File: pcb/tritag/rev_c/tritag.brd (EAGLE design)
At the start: 64.4 x 71.8 mm, 138 parts, among them J1 TC2030-JLINK-NL, J3 MICRO_USB_B_HIROSE_ZX62-B-5PA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, J4 BAT_HOLE, J5 BAT_HOLE, J6 TC2030-JLINK-NL, J7 CON_MICRO_SDDM3AT-SF-PEJM5, T1 HHM1595A1, U1 NRF52840, U12 SIP32510, U2 MCP73831, U3 FT232RQ, U4 MAX8887EZK33+T, U5 STM32F091CC, U6 SKY13317, U7 LXDC2HN18A, U8 DW1000, U9 LIS2DW12, X1 32MHz, X2 38.4M, X3 16M, X4 32.768kHz

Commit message: carrier board ready for layout
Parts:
- removed D3: SML-LX0404SIUPGUSB, leds:1MM_SQ_4PAD
- removed J6: TC2030-JLINK-NL, connector:TC2030-IDC-NL
- removed R15: 1k, passives:0402_RES
- removed R16: 100k, passives:0201_RES
- removed SJ2, SJ3, SJ4, SJ5: SOLDERJUMPERNC2, SparkFun-Passives:SJ_2S-NOTRACE
- added D2: SML-LX0404SIUPGUSB, leds:1MM_SQ_4PAD
- added GPIO0, GPIO1: TEST_POINT_0.040IN, headers:TESTPOINT_0.040IN
- added J2: TC2030-JLINK-NL, connector:TC2030-IDC-NL
- added R1: 270, passives:0402_RES
- added R6: 16k, passives:0402_RES
- added TP13, TP14: TEST-POINT, headers:PAD.03X.03
- added U$2: (no value), logos:UCB_CAL_50MIL
- C18, C21, C58: device passives:0603_CAP -> passives:0402_CAP
- C20, C22, C23, C24, C25, C26, C27, C28, C29, C30, C31, C32, C33, C34, C35, C36, C37, C38, C39, C40, C41, C42, C43, C44, C45, C46, C47, C48, C49, C50, C51, C52, C57: device passives:0201_CAP -> passives:0402_CAP
- C53: value 100nF -> 4.7uF; device passives:0201_CAP -> passives:0402_CAP
- C54: value 4.7uF -> 100nF; device passives:0201_CAP -> passives:0402_CAP
- C55: value 10nF -> 1uF; device passives:0201_CAP -> passives:0402_CAP
- C56: value 1uF -> 10nF; device passives:0201_CAP -> passives:0402_CAP
- R10: value 16k -> 11k; device passives:0201_RES -> passives:0402_RES
- R11, R12: value 11k -> 1k; device passives:0201_RES -> passives:0402_RES
- R14: value 1k -> 100k
- R9: value 270 -> 11k 1%; device passives:0201_RES -> passives:0402_RES
- TP5, TP6: value TEST_POINT_0.040IN -> TEST-POINT; device headers:TESTPOINT_0.040IN -> headers:PAD.03X.03
- moved A5 280.6 mm to (78.5, 29.1)
- moved A2.1 273.8 mm to (92.1, 29.1)
- moved A2 273.5 mm to (85.2, 29.1)
- moved C60 246.6 mm to (79.2, -15.7)
- moved A4 221.7 mm to (72.1, -7.49)
- moved C1 221.7 mm to (85.5, -10.3)
- moved C12 221.7 mm to (78.2, -6.73)
- moved C14 221.7 mm to (81.8, -6.73)
- moved C2 221.7 mm to (71.4, -13.1)
- moved C3 221.7 mm to (74.0, -13.1)
- moved C4 221.7 mm to (76.7, -13.1)
- moved C5 221.7 mm to (79.4, -13.1)
- moved C6 221.7 mm to (82.0, -13.1)
- moved C7 221.7 mm to (84.7, -13.1)
- moved C78 221.7 mm to (85.3, -6.73)
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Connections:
- removed net !FTDI_RESET: SJ3.2, U3.18
- removed net FTDI_VCCIO: SJ2.2, U3.1
- removed net N$28: D3.3, R15.1
- removed net N$29: D3.2, R13.1
- removed net RXD: SJ4.1, U3.2
- removed net TXD: SJ5.1, U3.30
- removed net VBAT_OK: U1.R24
- removed net VCC: C1.1, C11.1, C2.1, C3.1, C5.1, C6.1, C75.1, C76.1, D5.1, J1.1, R4.2, R5.2, SJ2.1, U1.A22, U1.AD14, U1.AD23, U1.B1, U1.W1, U1.Y2, U12.5, U12.6, U4.5, U9.10, U9.9
- new net N$12: C42.1, R6.2
- new net N$14: C44.1, R1.1, U8.12
- new net N$16: C43.1, R6.1, U8.8
- new net N$8: C41.1, R1.2
- new net NRF_GPIO_0: TP13.P$1, U1.AC11
- new net NRF_GPIO_1: TP14.P$1, U1.AD12
- new net NRF_SWO: J1.6, U1.AD22
- net !RST: now also U3.18; no longer SJ3.1
- net !STM_RST: now also J2.3; no longer J6.3
- net +1V8: now also C20.1, C24.1; no longer C20.P$1, C24.P$1
- net +3V3: now also C1.1, C11.1, C2.1, C3.1, C31.1, C32.1, C33.1, C34.1, C35.1, C36.1, C37.1, C38.1, C39.1, C40.1, C49.1, C5.1, C50.1, C51.1, C52.1, C53.1, C54.1, C55.1, C56.1, C6.1, C75.1, C76.1, D2.1, D5.1, J1.1, J2.1, R4.2, R5.2, U1.A22, U1.AD14, U1.AD23, U1.B1, U1.W1, U1.Y2, U12.5, U12.6, U3.1, U4.5, U9.10, U9.9; no longer C31.P$1, C32.P$1, C33.P$1, C34.P$1, C35.P$1, C36.P$1, C37.P$1, C38.P$1, C39.P$1, C40.P$1, C49.P$1, C50.P$1, C51.P$1, C52.P$1, C53.P$1, C54.P$1, C55.P$1, C56.P$1, D3.1, J6.1
- net DBG_RX: now also U3.30; no longer SJ5.2
- net DBG_TX: now also U3.2; no longer SJ4.2
- net DW_IRQ: now also R14.2; no longer R16.2
- net EXT_I2C_SCL: now also U1.AD8; no longer U1.A20, U1.AC9
- net EXT_I2C_SDA: no longer U1.B19
- net GND: now also C20.2, C22.2, C23.2, C24.2, C25.2, C26.2, C27.2, C28.2, C29.2, C30.2, C31.2, C32.2, C33.2, C34.2, C35.2, C36.2, C37.2, C38.2, C39.2, C40.2, C41.2, C42.2, C43.2, C44.2, C45.2, C46.2, C47.2, C48.2, C49.2, C50.2, C51.2, C52.2, C53.2, C54.2, C55.2, C56.2, C57.2, J2.5, R10.2, R14.1, R9.1, TP10.P$1; no longer C20.P$2, C22.P$2, C23.P$2, C24.P$2, C25.P$2, C26.P$2, C27.P$2, C28.P$2, C29.P$2, C30.P$2, C31.P$2, C32.P$2, C33.P$2, C34.P$2, C35.P$2, C36.P$2, C37.P$2, C38.P$2, C39.P$2, C40.P$2, C41.P$2, C42.P$2, C43.P$2, C44.P$2, C45.P$2, C46.P$2, C47.P$2, C48.P$2, C49.P$2, C50.P$2, C51.P$2, C52.P$2, C53.P$2, C54.P$2, C55.P$2, C56.P$2, C57.P$2, J6.5, R11.1, R12.2, R16.1, TP12.P$1
- net GPIO0: now also GPIO0.TESTPOINT; no longer TP5.TESTPOINT
- net GPIO1: now also GPIO1.TESTPOINT; no longer TP6.TESTPOINT
- net GPIO2: now also TP5.P$1, U5.29; no longer TP7.P$1, U5.21
- net GPIO3: now also TP6.P$1, U5.28; no longer TP8.P$1, U5.22
- net LED_BLUE: now also R13.2; no longer R15.2, TP10.P$1
- net LED_GREEN: now also R12.2, U5.41; no longer R14.2, TP9.P$1, U5.39
- net LED_RED: now also R11.2, U5.39; no longer R13.2, TP11.P$1, U5.41
- net N$21: now also U8.5; no longer C41.P$1
- net N$22: now also R10.1, U5.44; no longer C42.P$1, R10.2
- net N$23: now also D2.4, R12.1, TP7.P$1; no longer C44.P$1, R9.1, U8.12
- net N$24: now also D2.3, R13.1, TP9.P$1; no longer C43.P$1, R10.1, U8.8
- net N$25: now also D2.2, R11.1, TP8.P$1; no longer R11.2, U8.5
- net N$26: now also TP11.P$1, U8.36; no longer R12.1, U5.44
- net N$27: now also TP12.P$1, U8.35; no longer D3.4, R14.1
- net OSC_IN: now also C47.1; no longer C47.P$1
- net OSC_OUT: now also C48.1; no longer C48.P$1
- net STM_INTERRUPT: now also U1.AC21; no longer U1.B17
- net STM_SWCLK: now also J2.4; no longer J6.4
- net STM_SWDIO: now also J2.2; no longer J6.2
- net VDDCLK: now also C26.1; no longer C26.P$1
- net VDDDIG: now also C22.1, C23.1; no longer C22.P$1, C23.P$1
- net VDDIF: now also C29.1; no longer C29.P$1
- net VDDIO: now also C28.1, C57.1; no longer C28.P$1, C57.P$1
- net VDDMS: now also C25.1; no longer C25.P$1
- net VDDSYN: now also C27.1; no longer C27.P$1
- net VDDVCO: now also C30.1; no longer C30.P$1
- net XTAL1: now also C46.1; no longer C46.P$1
- net XTAL2: now also C45.1; no longer C45.P$1
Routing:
- net +3V3: track 87.1 -> 256.6 mm, vias 5 -> 13
- net VCC: track 50.8 -> 0.00 mm, vias 4 -> 0
- net VBAT: track 46.7 -> 0.00 mm
- net N$5: track 28.2 -> 0.00 mm, vias 3 -> 0
- net VUSB: track 24.1 -> 0.00 mm, vias 1 -> 0
- net EXT_I2C_SCL: track 20.4 -> 0.00 mm, vias 1 -> 0
- net EXT_I2C_SDA: track 19.4 -> 0.00 mm, vias 1 -> 0
- net STM_INTERRUPT: track 17.6 -> 0.00 mm, vias 1 -> 0
- net LED_RED: track 14.8 -> 1.69 mm, vias 2 -> 0
- net LED_BLUE: track 13.5 -> 1.48 mm, vias 2 -> 0
- net LED_GREEN: track 12.2 -> 1.37 mm, vias 2 -> 0
- net GND: track 96.6 -> 105.1 mm, vias 46 -> 204
- net RF2: track 7.93 -> 15.4 mm
- net RF1: track 6.40 -> 13.8 mm
- net N$16: track 0.00 -> 4.89 mm
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- added copper zone on layer 1, net N$3
- added copper zone on layer 1, net RF3
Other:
- board size 64.4 x 71.8 mm -> 66 x 48.9 mm
- board text added: "17/07/2018"
- board text added: "Andreas Biri, Pat Pannuto"
- board text added: "C"
- board text added: "G"
- board text added: "GND"
- board text added: "IO2"
- board text added: "IO3"
- board text added: "R"
- board text added: "SquarePoint"
- board text added: "v3.1"
- board text removed: "13/07/2018"
- board text removed: "2018/07/14"
- board text removed: "Andreas Biri"

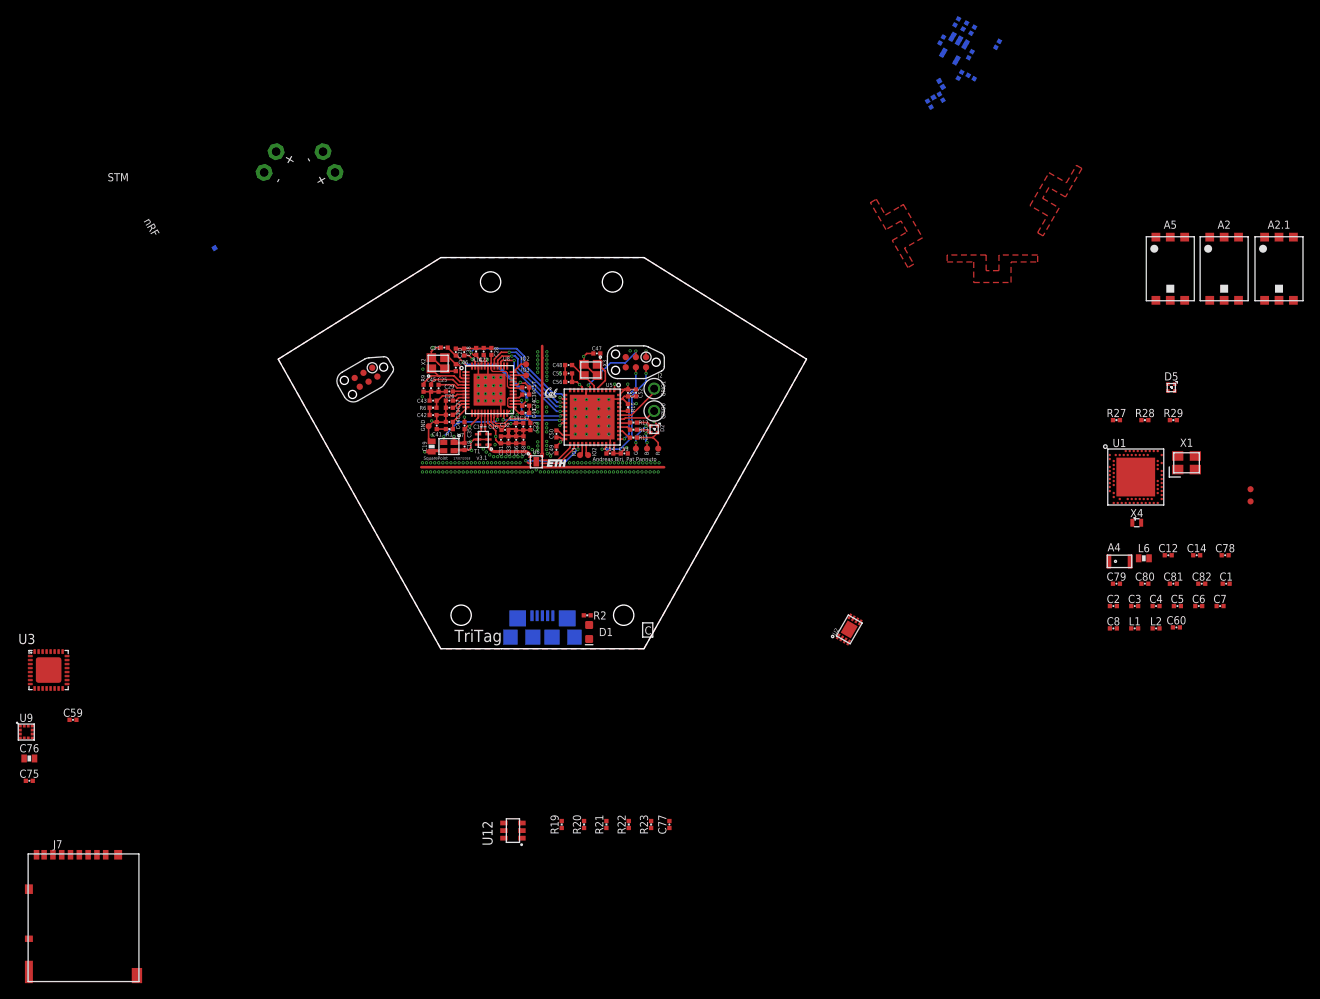
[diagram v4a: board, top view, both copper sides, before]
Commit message: Carrier ready for routing
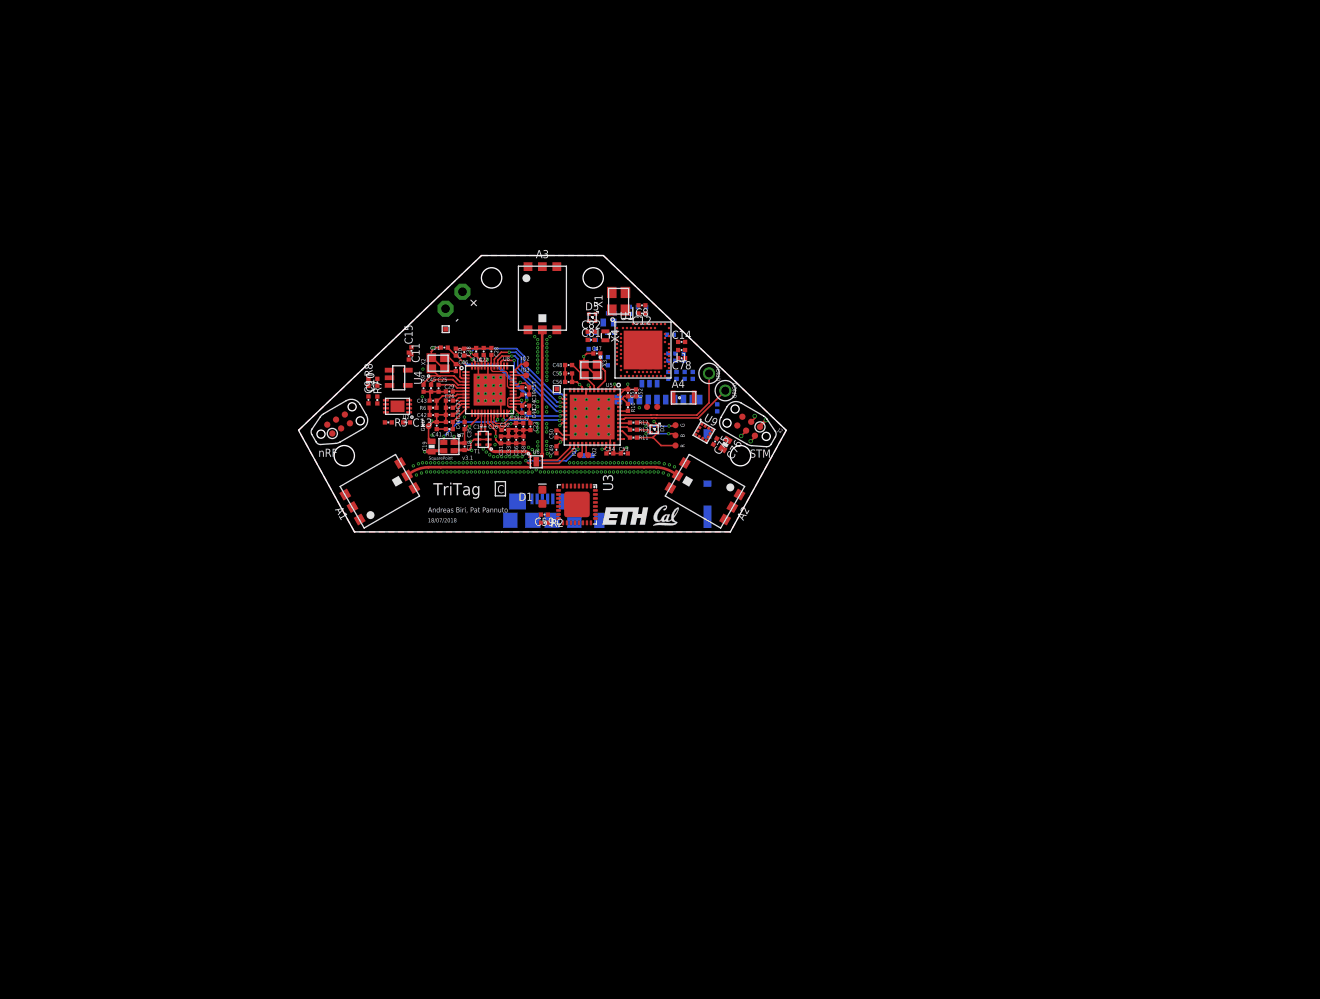
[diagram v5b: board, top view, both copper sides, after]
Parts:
- removed A2.1, A5: TAIYO-YUDEN-AH086M, chips:TAIYO-YUDEN-AH086M
- removed J4: BAT_HOLE, connector:BATTERY_HOLE
- removed R4, R5: DNP, passives:0402_RES
- removed U$1: (no value), logos:ETH_100MIL
- removed U$2: (no value), logos:UCB_CAL_50MIL
- added A1, A3: TAIYO-YUDEN-AH086M, chips:TAIYO-YUDEN-AH086M
- added U$3: (no value), logos:ETH_200MIL
- added U$4: (no value), logos:UCB_CAL_100MIL
- moved C75 95.6 mm to (21.6, 7.49), turned to 240 degrees
- moved C76 95.4 mm to (22.9, 7.11), turned to 240 degrees
- moved U9 92.6 mm to (20.2, 8.64), turned to 330 degrees
- moved J7 91.8 mm to (14.2, 12.8), flipped to the bottom
- moved C10 88.3 mm to (-20.6, 14.9), flipped to the top, turned to 90 degrees
- moved R8 87.4 mm to (-21.7, 14.9), flipped to the top, turned to 270 degrees
- moved C9 87.4 mm to (-21.7, 12.7), flipped to the top, turned to 90 degrees
- moved R7 87.1 mm to (-20.6, 12.7), flipped to the top, turned to 90 degrees
- moved R3 83.6 mm to (-19.3, 9.87), flipped to the top, turned to 180 degrees
- moved C13 82.7 mm to (-17.0, 9.87), flipped to the top, turned to 180 degrees
- moved C82 82.6 mm to (6.10, 21.2)
- moved C1 82.0 mm to (10.9, 23.9), flipped to the bottom, turned to 90 degrees
- moved U4 80.7 mm to (-18.0, 15.5), flipped to the top, turned to 270 degrees
- moved C6 80.5 mm to (7.75, 18.0), flipped to the bottom
- moved C15 79.1 mm to (-16.4, 18.8), flipped to the top, turned to 90 degrees
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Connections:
- removed net INTERRUPT: U5.12
- net +3V3: no longer R4.2, R5.2
- net EXT_I2C_SCL: no longer R5.1
- net EXT_I2C_SDA: no longer R4.1
- net GND: no longer J4.N
- net RF1: now also A1.A; no longer A5.A
- net RF2: now also A2.A; no longer A2.1.A
- net RF3: now also A3.A; no longer A2.A
- net STM_INTERRUPT: now also U5.12
- net VBAT: no longer J4.P
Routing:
- net +3V3: track 256.6 -> 227.1 mm
- net !STM_RST: track 9.28 -> 25.7 mm
- net GPIO0: track 4.79 -> 14.7 mm
- net GPIO1: track 6.02 -> 15.6 mm
- net STM_SWCLK: track 10.2 -> 17.3 mm, vias 2 -> 1
- net STM_SWDIO: track 14.8 -> 21.1 mm
- net GND: track 105.1 -> 102.8 mm, vias 204 -> 219
- net RF1: track 13.8 -> 15.8 mm
- net RF3: track 13.9 -> 15.9 mm
- net RF2: track 15.4 -> 17.3 mm
- net N$24: track 4.43 -> 6.29 mm
- net N$25: track 4.53 -> 6.10 mm
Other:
- board size 66 x 48.9 mm -> 61 x 34.5 mm
- board text added: "18/07/2018"
- board text removed: "17/07/2018"

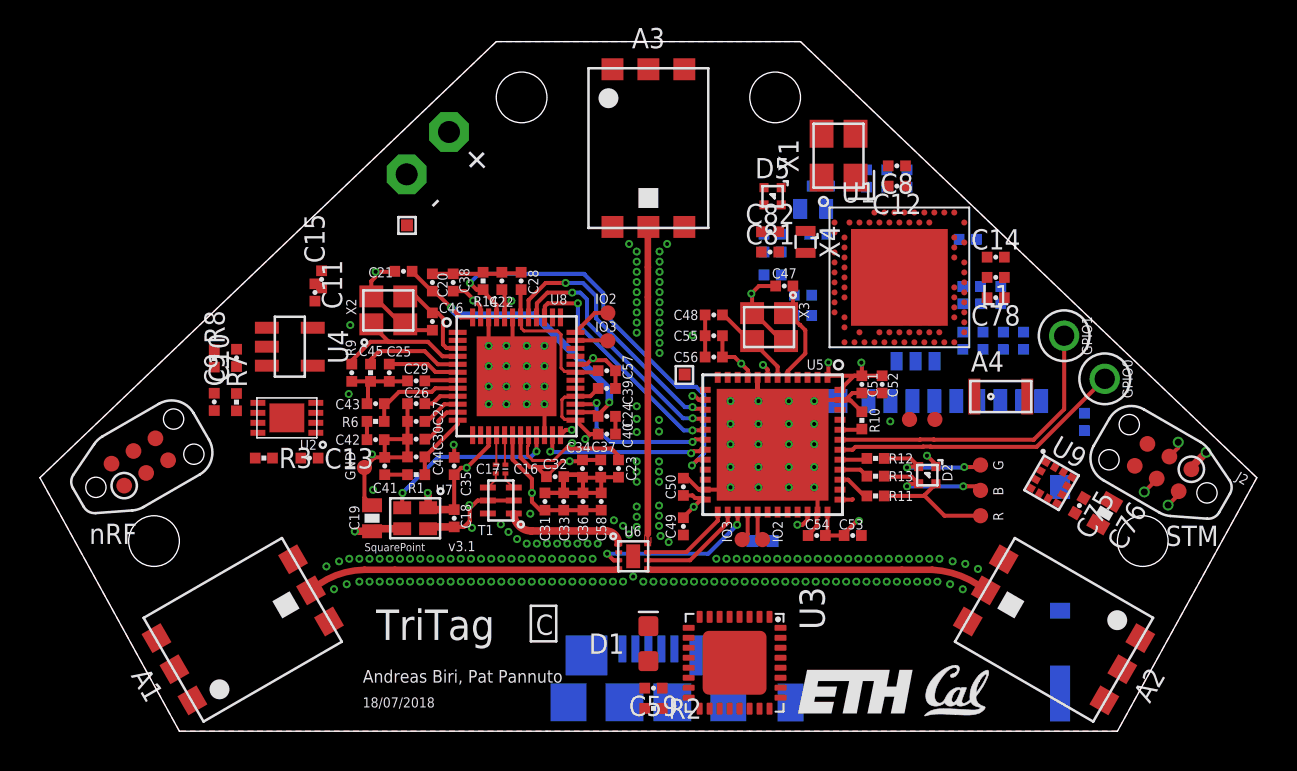
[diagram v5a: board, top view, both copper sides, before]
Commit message: carrier routed apart from nRF
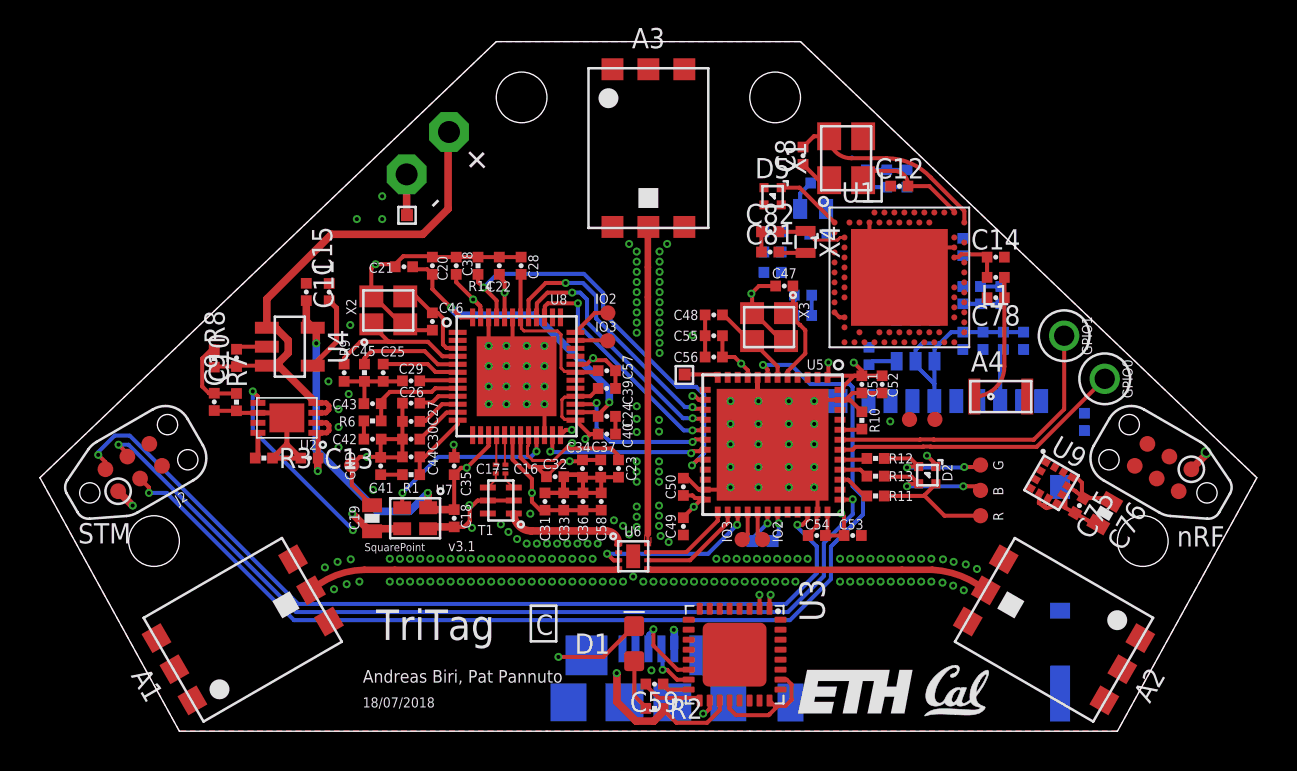
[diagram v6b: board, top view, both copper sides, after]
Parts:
- moved J2 51.6 mm to (-25.8, 9.40), turned to 30 degrees
- moved J1 51.3 mm to (25.8, 9.40), turned to 150 degrees
- moved C8 4.73 mm to (7.75, 25.0), turned to 90 degrees
- moved R19 4.18 mm to (11.0, 15.0)
- moved C38 0.85 mm to (-9.63, 19.5)
- moved C20 0.84 mm to (-10.8, 19.5)
- moved R14 0.80 mm to (-8.53, 19.5)
- moved C22 0.77 mm to (-7.47, 19.5)
- moved C28 0.76 mm to (-6.38, 19.5)
- moved C15 0.74 mm to (-16.0, 18.2)
- moved D1 0.71 mm to (-0.71, 0.58)
- moved TP10 0.65 mm to (-14.9, 9.53)
- moved TP4 0.51 mm to (-12.1, 22.0)
- moved C7 0.46 mm to (15.7, 20.4), turned to 270 degrees
- moved C11 0.43 mm to (-17.1, 18.2)
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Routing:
- net +3V3: track 227.1 -> 278.4 mm, vias 13 -> 16
- net GND: track 102.8 -> 147.1 mm, vias 219 -> 217
- net VUSB: track 0.00 -> 39.2 mm, vias 0 -> 3
- net !STM_RST: track 25.7 -> 54.7 mm
- net N$5: track 0.00 -> 28.4 mm, vias 0 -> 3
- net STM_SWCLK: track 17.3 -> 45.4 mm, vias 1 -> 2
- net VBAT: track 0.00 -> 27.1 mm
- net STM_SWDIO: track 21.1 -> 45.3 mm
- net N$55: track 0.00 -> 10.9 mm
- net N$18: track 0.00 -> 10.4 mm
- net !RST: track 0.00 -> 8.38 mm, vias 0 -> 1
- net N$17: track 0.00 -> 6.59 mm
- net N$19: track 0.00 -> 5.77 mm
- net D+: track 0.00 -> 4.17 mm, vias 0 -> 1
- net BATIN: track 0.00 -> 4.05 mm
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
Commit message: carrier board finalized, HW revision completed
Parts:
- moved TP13 15.8 mm to (4.83, 25.3)
- moved TP14 15.7 mm to (6.22, 25.3)
- moved C12 4.82 mm to (7.85, 24.4), turned to 270 degrees
- moved C8 3.06 mm to (10.4, 26.6), turned to 0 degrees
- moved C6 2.35 mm to (8.46, 15.8), flipped to the top, turned to 270 degrees
- moved R27 1.78 mm to (6.22, 21.0)
- moved R28 1.27 mm to (6.22, 18.9)
- moved R29 1.27 mm to (6.22, 19.9)
- moved C3 0.92 mm to (8.46, 17.6), flipped to the top, turned to 90 degrees
- moved C77 0.76 mm to (18.8, 15.0)
- moved R21 0.76 mm to (15.7, 15.0)
- moved R22 0.76 mm to (16.8, 15.0)
- moved R23 0.76 mm to (17.8, 15.0)
- moved X1 0.66 mm to (10.4, 24.4), turned to 0 degrees
- moved R19 0.47 mm to (10.9, 14.5), turned to 0 degrees
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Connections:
- removed net !RST: U1.AC13, U3.18
- removed net NRF_SWO: J1.6, U1.AD22
- removed net SCK: U1.U1
- removed net VSEC: U1.A8
- removed net VSOL: U1.B9
- new net !FT_RST: U1.P2, U3.18
- net !NRF_CS_IMU: now also U1.AC11; no longer U1.AC17
- net !NRF_CS_SD: now also U1.AC13; no longer U1.AC15
- net !SD_DETECT: now also U1.AD22; no longer U1.AD20
- net BATIN: no longer U1.P23
- net DBG_RX: now also U1.M2; no longer U1.G1
- net DBG_TX: now also U1.T2; no longer U1.H2
- net EXT_I2C_SCL: now also U1.R1; no longer U1.AD8
- net EXT_I2C_SDA: now also U1.U1; no longer U1.AD10
- net LED_NRF_BLUE: now also U1.J1; no longer U1.K2
- net LED_NRF_RED: now also U1.K2; no longer U1.J1
- net NRF_GPIO_0: now also U1.H2; no longer U1.AC11
- net NRF_GPIO_1: now also U1.G1; no longer U1.AD12
- net NRF_IMU_INT1: now also U1.AD18; no longer U1.AD16
- net NRF_IMU_INT2: now also U1.AD20; no longer U1.AD18
- net NRF_MISO: now also U1.AD10; no longer U1.R1
- net NRF_MOSI: now also U1.AD8; no longer U1.N1
- net NRF_SCK: now also U1.AD12
- net SD_EN: now also U1.AC9; no longer U1.AC19
- net STM_INTERRUPT: now also U1.N1; no longer U1.AC21
- net VBAT: no longer U1.A10
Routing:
- net !FT_RST: track 0.00 -> 28.5 mm, vias 0 -> 3
- net DBG_RX: track 0.00 -> 23.7 mm, vias 0 -> 3
- net DBG_TX: track 0.70 -> 22.3 mm, vias 1 -> 3
- net NRF_GPIO_0: track 0.00 -> 20.7 mm, vias 0 -> 2
- net !SD_DETECT: track 0.00 -> 18.9 mm, vias 0 -> 2
- net NRF_GPIO_1: track 0.00 -> 18.4 mm, vias 0 -> 2
- net NRF_SWDCLK: track 0.00 -> 16.9 mm, vias 0 -> 2
- net EXT_I2C_SCL: track 1.77 -> 18.3 mm, vias 1 -> 2
- net NRF_SWDIO: track 0.00 -> 16.1 mm, vias 0 -> 2
- net NRF_MOSI: track 0.00 -> 14.9 mm, vias 0 -> 3
- net EXT_I2C_SDA: track 1.60 -> 16.0 mm, vias 1 -> 2
- net NRF_IMU_INT2: track 0.00 -> 12.7 mm, vias 0 -> 2
- net N$9: track 1.02 -> 13.6 mm, vias 0 -> 2
- net NRF_IMU_INT1: track 0.00 -> 12.5 mm, vias 0 -> 2
- net !NRF_CS_IMU: track 0.00 -> 12.3 mm, vias 0 -> 2
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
